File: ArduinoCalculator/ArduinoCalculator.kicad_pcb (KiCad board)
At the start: 2 copper layers, 1 part, among them U1 NORA-W106-00B

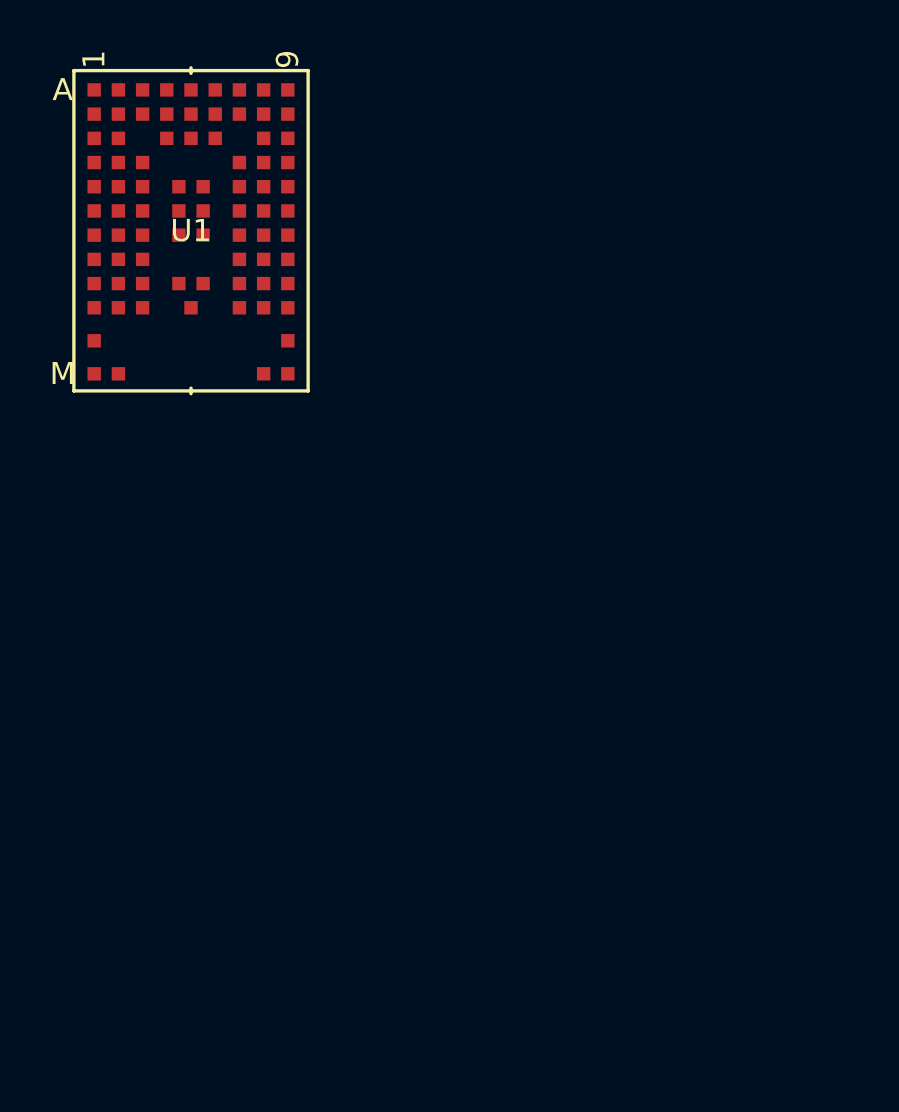
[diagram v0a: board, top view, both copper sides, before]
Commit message: added NORA model
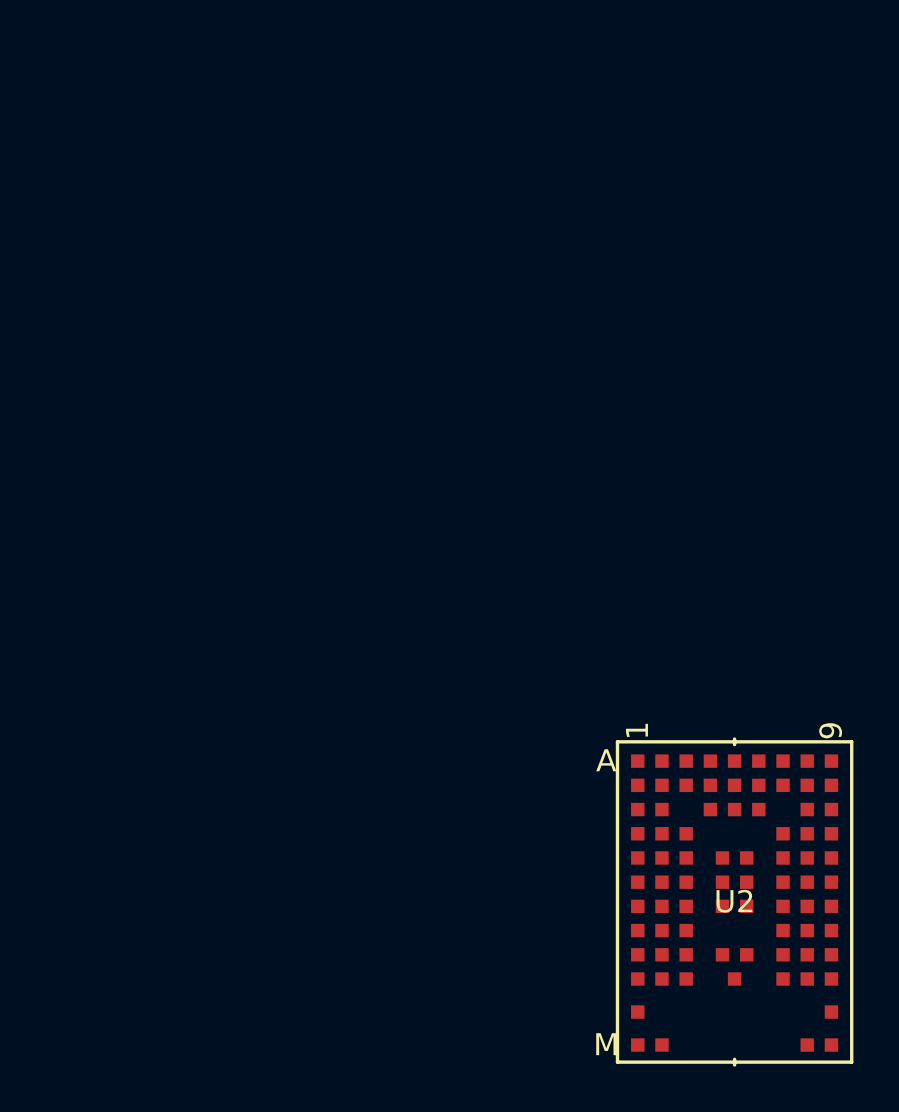
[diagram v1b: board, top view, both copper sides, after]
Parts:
- removed U1: NORA-W106-00B, footprints:NORA-W10_UBL
- added U2: NORA-W106-10B, footprints:NORA-W10_UBL, F.Cu at (94.6, 115.0)

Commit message: adde libs
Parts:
- added DS1: WC1602A, Display:WC1602A, F.Cu at (48.0, 47.5)
- added J1: Conn_01x04_Socket, Connector_PinHeader_2.54mm:PinHeader_1x04_P2.54mm_Vertical, F.Cu at (158.0, 83.9)
- added SW1: Push_Button, PCM_Switch_Keyboard_Cherry_MX:SW_Cherry_MX_PCB, F.Cu at (149.1, 119.5)

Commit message: slakd
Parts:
- added J2: USB_C_Receptacle_USB2.0_16P, Connector_USB:USB_C_Receptacle_GCT_USB4105-xx-A_16P_TopMnt_Horizontal, F.Cu at (206.5, 149.0)
- added J3: PINHD_2x5_Male, Connector_PinHeader_2.54mm:PinHeader_2x05_P2.54mm_Vertical, F.Cu at (178.7, 104.9)
- moved DS1 129.1 mm to (177.0, 53.0)
- moved U2 92.7 mm to (182.5, 144.5)
- moved SW1 82.2 mm to (230.5, 130.5)
- moved J1 50.0 mm to (207.0, 94.0)
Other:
- board outline added: 83 x 103 mm
